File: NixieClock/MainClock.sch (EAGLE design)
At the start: 60 parts, among them IC1 MEGA8-P, IC2 74141N, Q1 MPSA 42, Q12 MPSA 92, Q13 MPSA 42, Q14 MPSA 42, Q2 MPSA 42, Q3 MPSA 42, Q4 MPSA 42, Q5 MPSA 92, Q6 MPSA 92, Q7 MPSA 92, Q8 MPSA 92, Q9 MPSA 92

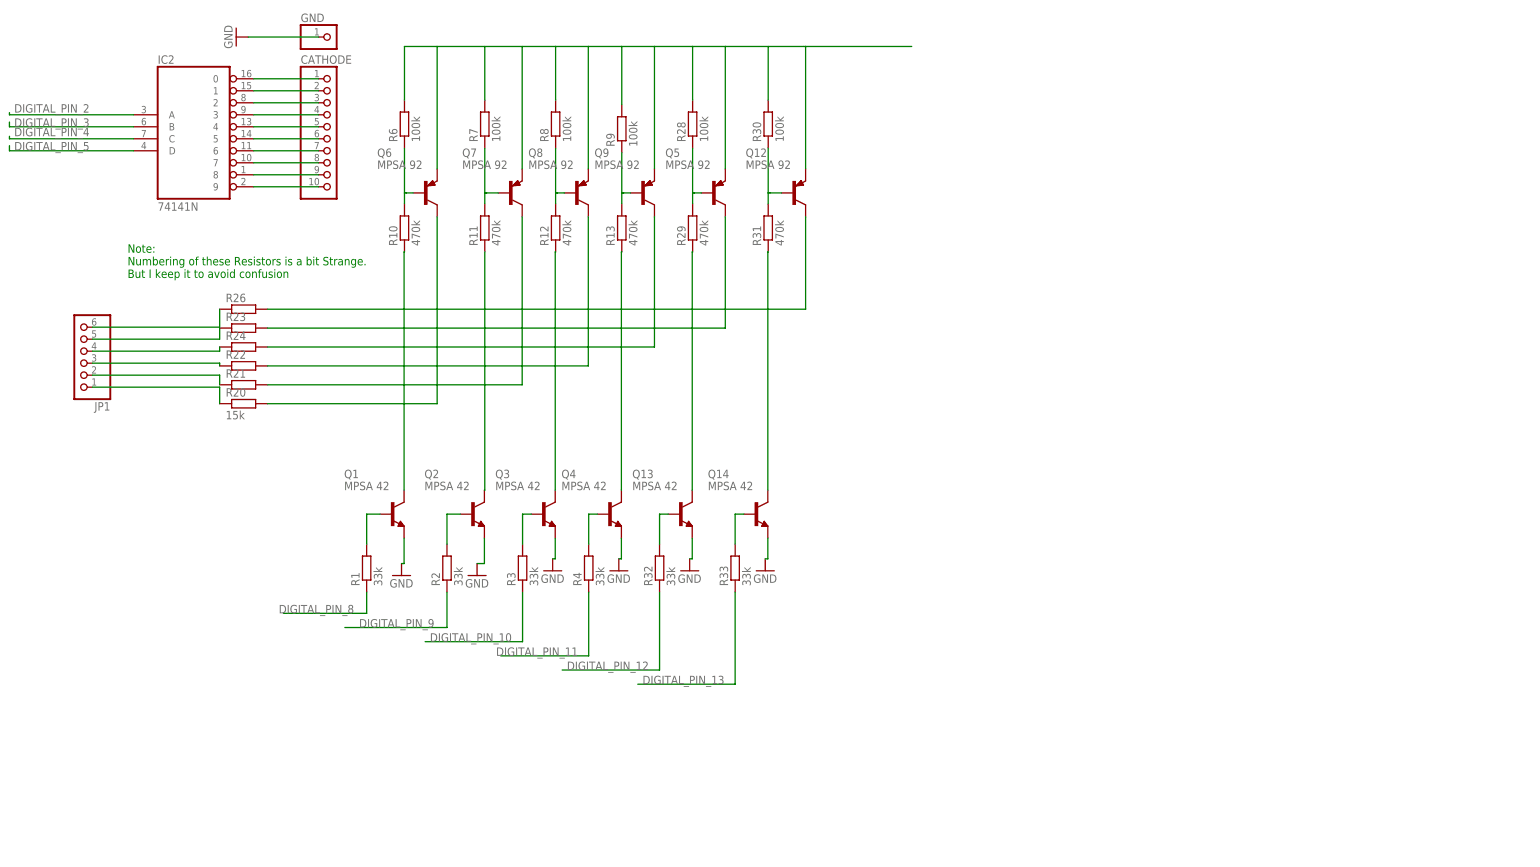
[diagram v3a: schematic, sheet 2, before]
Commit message: Finished 2nd Sheet. Still have a few ToDos though
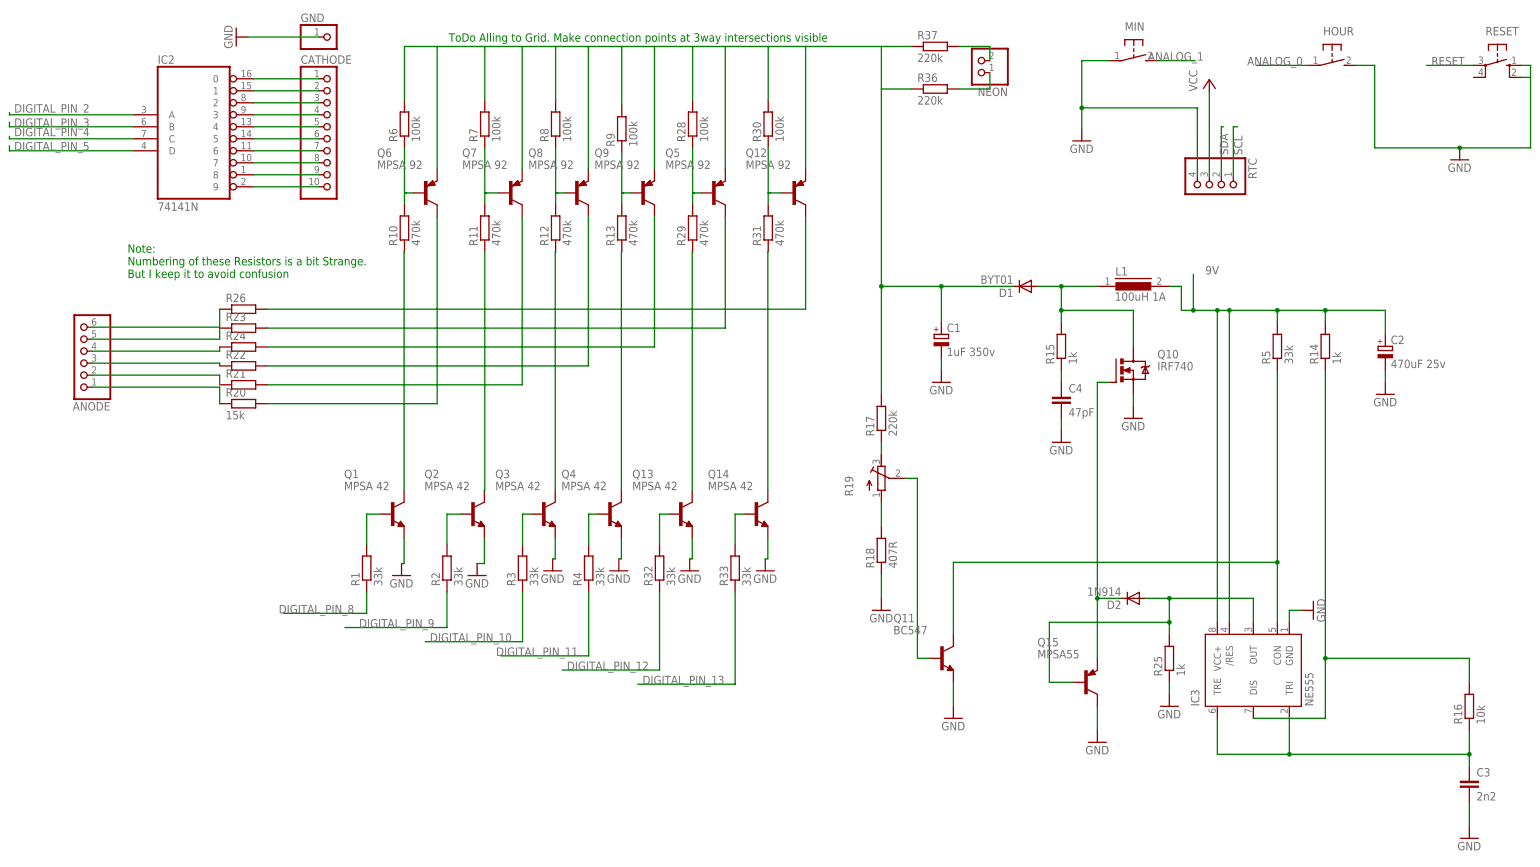
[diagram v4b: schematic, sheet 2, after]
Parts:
- added C1: 1uF 350v, resistor:CPOL-EUE5-10.5
- added C2: 470uF 25v, resistor:CPOL-EUE5-10.5
- added C3: 2n2, resistor:C-EU025-024X044
- added C4: 47pF, resistor:C-EU025-024X044
- added D1: BYT01, diode:BYT01
- added D2: 1N914, diode:1N4446
- added HOUR, MIN: (no value), switch-omron:31-XX
- added IC3: NE555, st-microelectronics:NE555
- added L1: 100uH 1A, inductors:MESC26
- added NEON: (no value), pinhead:PINHD-1X2
- added Q10: IRF740, transistor-power:IRF740
- added Q11: BC547, transistor:BC547
- added Q15: MPSA55, transistor:MPSA56-PNP-TO92-BCE
- added R14, R15, R25: 1k, resistor:R-EU_0309/10
- added R16: 10k, resistor:R-EU_0309/10
- added R17, R36, R37: 220k, resistor:R-EU_0309/10
- added R18: 407R, resistor:R-EU_0309/10
- added R19: (no value), resistor:R-TRIMM3339P
- added R5: 33k, resistor:R-EU_0309/10
- added RESET: (no value), switch-omron:10-XX
- added RTC: (no value), pinhead:PINHD-1X4
- renumbered JP1 to ANODE
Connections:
- new net N$52: NEON.2, R37.2
- new net N$53: NEON.1, R36.2
- new net N$54: C3.1, IC3.TRE, IC3.TRI, R16.1
- new net N$56: D1.A, L1.1, Q10.D, R15.2
- new net N$57: C4.1, R15.1
- new net N$58: IC3.DIS, R14.1, R16.2
- new net N$59: IC3.CON, Q11.C, R5.1
- new net N$60: R18.2, R19.A
- new net N$61: R17.1, R19.E
- new net N$62: D2.A, IC3.OUT, Q15.B, R25.2
- new net N$63: D2.C, Q10.G, Q15.E
- new net N$64: Q11.B, R19.S
- new net N$66: C1.+, D1.C, R17.2, R36.1
- new net VCC: RTC.3
- net 9V: now also C2.+, IC3./RES, IC3.VCC+, L1.2, R14.2, R5.2
- net ANALOG_0: now also HOUR.P
- net ANALOG_1: now also MIN.S
- net GND: now also C1.-, C2.-, C3.2, C4.2, HOUR.S, IC3.GND, MIN.P, Q10.S, Q11.E, Q15.C, R18.1, R25.1, RESET.S, RESET.S1, RTC.4
- net N$41: now also R37.1
- net RESET: now also RESET.P
- net SCL: now also RTC.1
- net SDA: now also RTC.2
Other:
- note added: "//TODO what about D5?"
- note added: "ToDo Alling to Grid. Make connection points at 3way intersections visible"

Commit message: Resolved ToDOs
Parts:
- removed OFF/ON/OFF_SUPPOSED: TL36PO, switch:TL36PO
- added OFF/ON: (no value), switch:255SB
- 12-35V/9V: value TL36PO -> (none); device switch:TL36PO -> switch:255SB
- C5, C6: device resistor:CPOL-EUE2-4 -> resistor:C-EU025-025X050
- R19: value (none) -> 1k
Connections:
- removed net 5V: C7.+, IC1.AREF, IC1.AVCC, IC1.VCC@1, L7805CV.OUT, R27.1, R35.1
- removed net N$41: Q12.E, Q5.E, Q6.E, Q7.E, Q8.E, Q9.E, R28.2, R30.2, R37.1, R6.2, R7.2, R8.2, R9.2
- removed net N$66: C1.+, D1.C, R17.2, R36.1
- new net N$34: C1.+, D1.C, Q12.E, Q5.E, Q6.E, Q7.E, Q8.E, Q9.E, R17.2, R28.2, R30.2, R36.1, R37.1, R6.2, R7.2, R8.2, R9.2
- net GND: now also C5.2, C6.1; no longer C5.-, C6.+
- net N$1: now also C6.2; no longer C5.+
- net N$2: now also C5.1; no longer C6.-
- net N$6: now also OFF/ON.P; no longer OFF/ON/OFF_SUPPOSED.P
- net N$7: now also OFF/ON.S; no longer OFF/ON/OFF_SUPPOSED.S
- net RESET: now also RESET.P1
- net VCC: now also C7.+, IC1.AREF, IC1.AVCC, IC1.VCC@1, L7805CV.OUT, R27.1, R35.1
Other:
- note added: "ToDo Alling to Grid. Make connection points at 3way intersections visible -> Done but because Eagle always starts with inch it got a bit crooked but now all connections are set right."
- note added: "ToDo c5,c6 not polarized -> Replaced by right transistors"
- note added: "ToDo what about D5? ->old D4 and D5 have been replaced by D4"
- note added: "ToDo: Find right switch: Used Switch which I think is right, but am not entirely sure"
- note removed: "//TODO what about D5?"
- note removed: "ToDo Alling to Grid. Make connection points at 3way intersections visible"
- note removed: "ToDo c5,c6 nicht gepoolt?"
- note removed: "ToDo: Find right switch"
- moved on the sheet: 9V/12-35V-DC-IN, ANODE, C1, C3, C7, D1, NEON, POWER_LED, Q12, Q5, Q6, Q7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

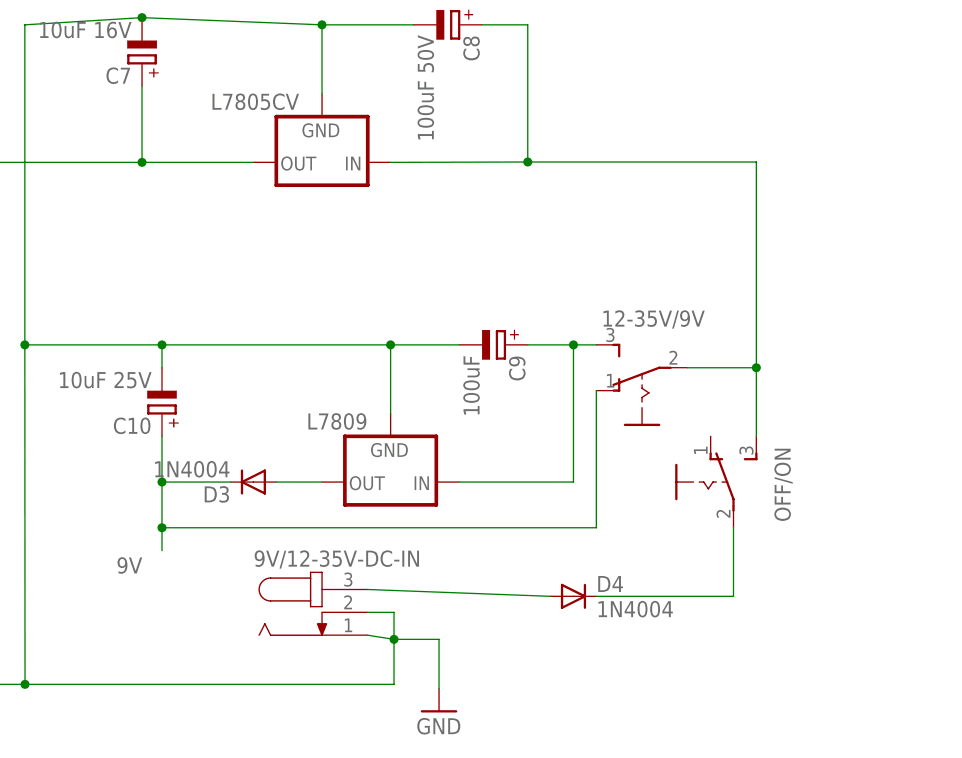
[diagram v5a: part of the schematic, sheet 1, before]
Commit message: Placed half of the components
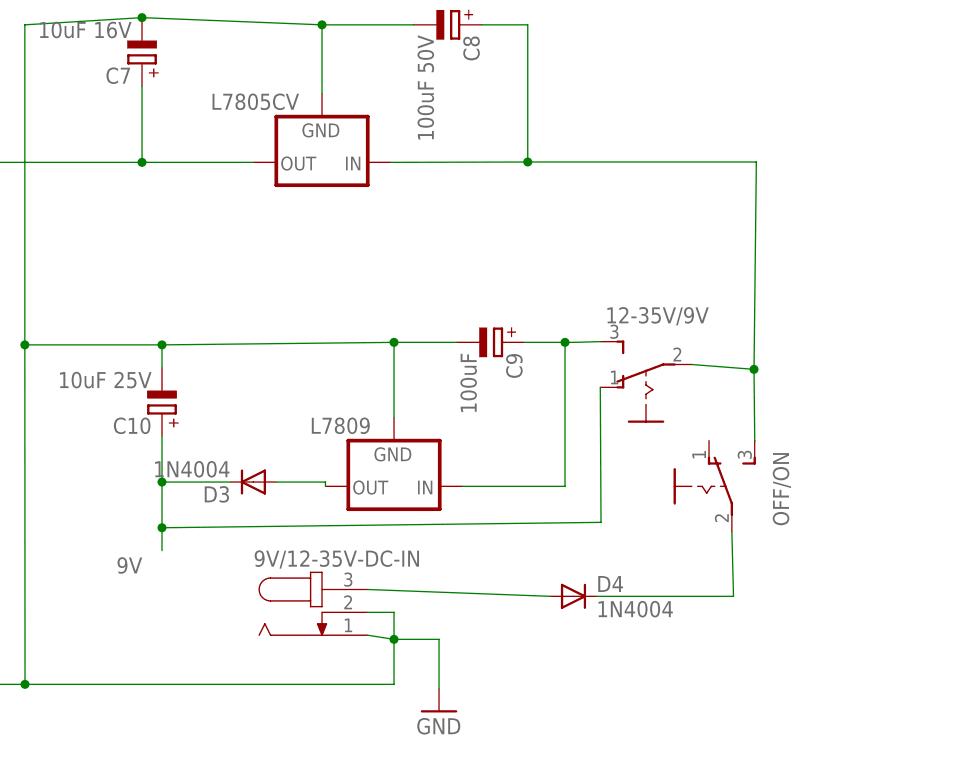
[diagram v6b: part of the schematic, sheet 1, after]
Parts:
- added +180V(TEST): (no value), pinhead:PINHD-1X1
- L7805CV, L7809: device v-reg:78XXL -> v-reg:78XXS
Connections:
- net N$34: now also +180V(TEST).1
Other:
- moved on the sheet: 12-35V/9V, OFF/ON
